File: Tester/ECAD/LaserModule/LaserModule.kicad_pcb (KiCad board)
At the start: 2 copper layers, 16 parts, among them J1 Conn_01x04_Male, Q1 ZXMP6A17G, U1 MCP4716, U2 AD8601

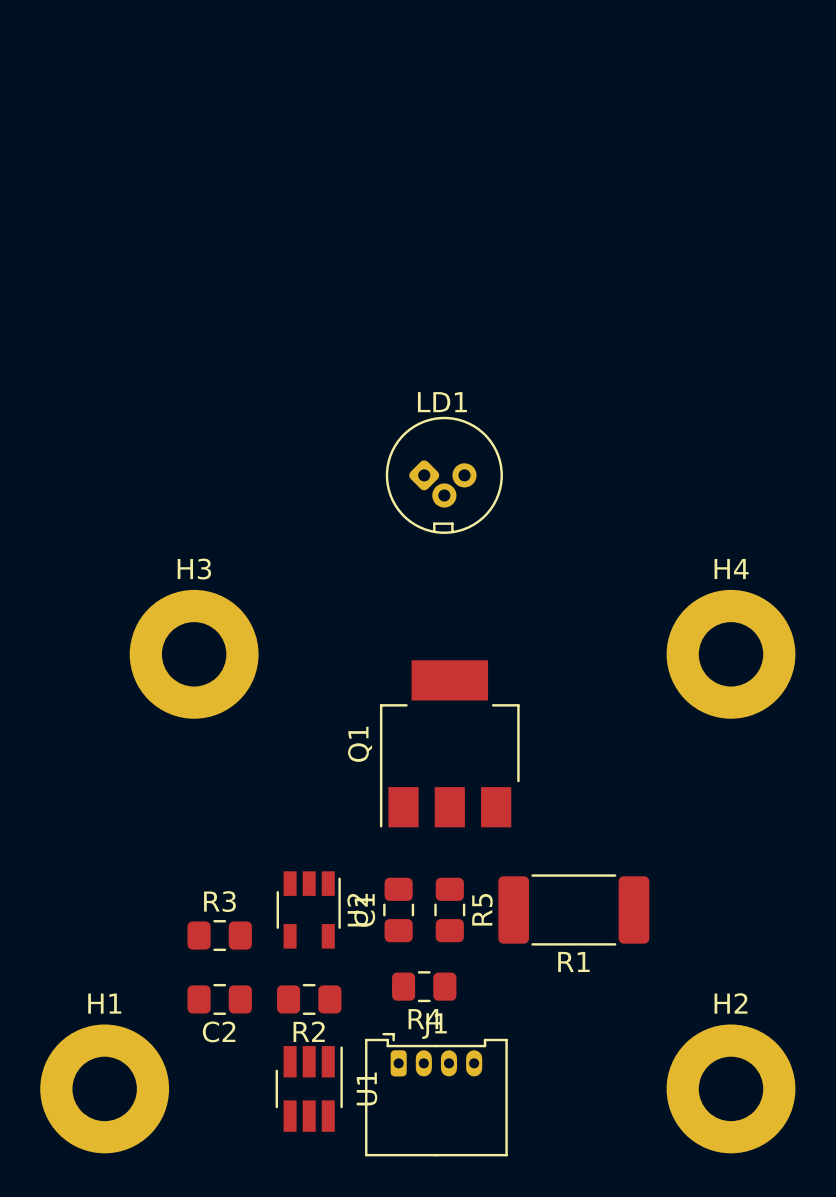
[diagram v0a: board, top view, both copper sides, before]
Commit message: Progressed laser module.
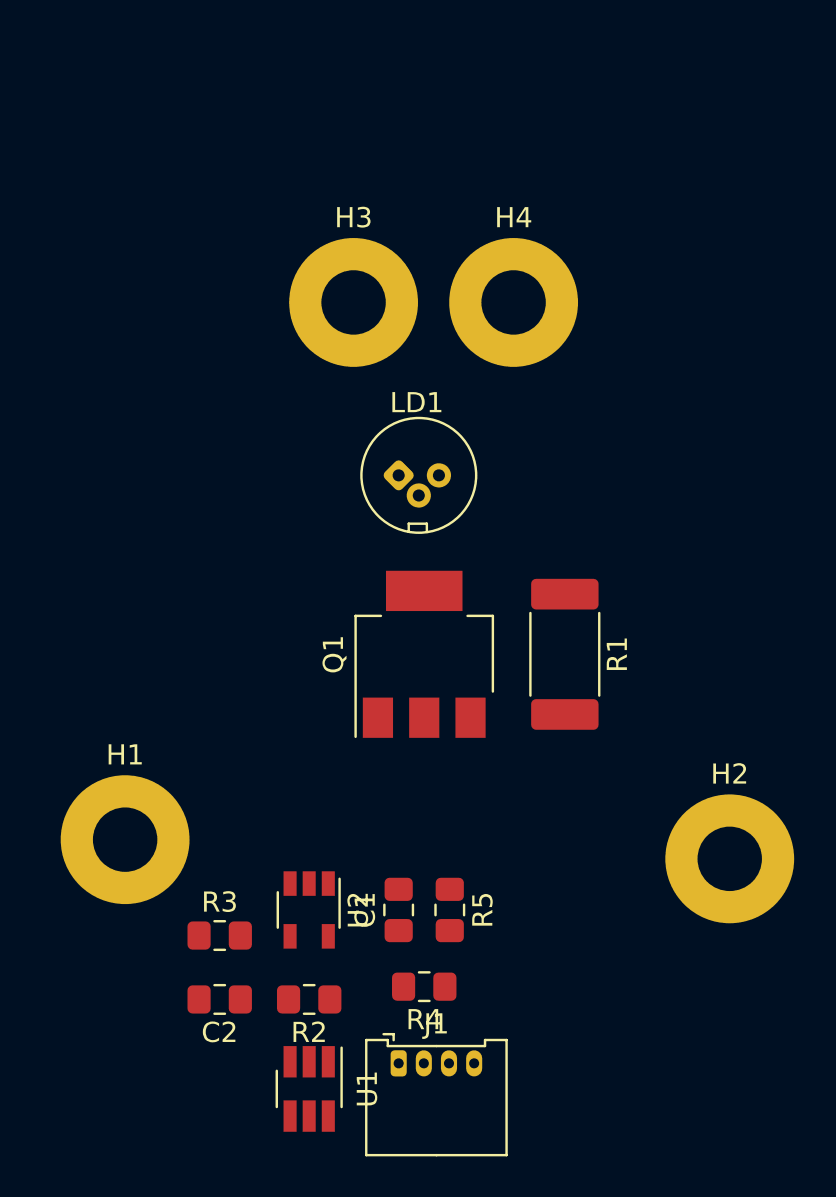
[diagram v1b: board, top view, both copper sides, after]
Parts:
- moved H4 20.5 mm to (147.3, 61.3)
- moved H3 19.2 mm to (139.4, 61.3)
- moved R1 12.7 mm to (149.9, 78.7), turned to 270 degrees
- moved H1 12.4 mm to (128.0, 87.9)
- moved H2 11.4 mm to (158.1, 88.9)
- moved Q1 4.62 mm to (142.9, 78.7)
- moved LD1 1.27 mm to (141.6, 69.8)
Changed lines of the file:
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@@
     (add_net "Net-(LD1-Pad1)")
+  )
+  (module MountingHole:MountingHole_3.2mm_M3_Pad (layer F.Cu)
+    (at 147.315001 61.260001)
+    (descr "Mounting Hole 3.2mm, M3")
+    (tags "mounting hole 3.2mm m3")
+    (attr virtual)
+    (fp_text reference H4 (at 0 -4.2) (layer F.SilkS)
+      (effects (font (size 1 1) (thickness 0.15)))
+    )
+    (fp_text value MountingHole (at 0 4.2) (layer F.Fab)
+      (effects (font (size 1 1) (thickness 0.15)))
+    )
+    (fp_circle (center 0 0) (end 3.45 0) (layer F.CrtYd) (width 0.05))
+    (fp_circle (center 0 0) (end 3.2 0) (layer Cmts.User) (width 0.15))
+    (fp_text user %R (at 0.3 0) (layer F.Fab)
+      (effects (font (size 1 1) (thickness 0.15)))
+    )
+    (pad 1 thru_hole circle (at 0 0) (size 6.4 6.4) (drill 3.2) (layers *.Cu *.Mask))
+  )
+  (module MountingHole:MountingHole_3.2mm_M3_Pad (layer F.Cu)
+    (at 139.365001 61.260001)
+    (descr "Mounting Hole 3.2mm, M3")
+    (tags "mounting hole 3.2mm m3")
+    (attr virtual)
+    (fp_text reference H3 (at 0 -4.2) (layer F.SilkS)
+      (effects (font (size 1 1) (thickness 0.15)))
+    )
+    (fp_text value MountingHole (at 0 4.2) (layer F.Fab)
+      (effects (font (size 1 1) (thickness 0.15)))
+    )
+    (fp_circle (center 0 0) (end 3.45 0) (layer F.CrtYd) (width 0.05))
+    (fp_circle (center 0 0) (end 3.2 0) (layer Cmts.User) (width 0.15))
+    (fp_text user %R (at 0.3 0) (layer F.Fab)
+      (effects (font (size 1 1) (thickness 0.15)))
+    )
+    (pad 1 thru_hole circle (at 0 0) (size 6.4 6.4) (drill 3.2) (layers *.Cu *.Mask))
   )
   (module Package_TO_SOT_SMD:SOT-23-6_Handsoldering (layer F.Cu)
@@
   )
   (module OptoDevice:LaserDiode_TO18-D5.6-3 (layer F.Cu)
-    (at 142.875 69.85)
+    (at 141.605 69.85)
     (descr "Laser Diode, TO18-like (D=5.6mm), 3pin")
     (tags "Laser Diode TO18-like")
@@
   )
   (module Resistor_SMD:R_2512_6332Metric_Pad1.52x3.35mm_HandSolder (layer F.Cu)
-    (at 150.3075 91.44 180)
+    (at 149.86 78.74 270)
     (descr "Resistor SMD 2512 (6332 Metric), square (rectangular) end terminal, IPC_7351 nominal with elongated pad for handsoldering. (Body size source: http://www.tortai-tech.com/upload/download/2011102023233369053.pdf), generated with kicad-footprint-generator")
     (tags "resistor handsolder")
     (attr smd)
-    (fp_text reference R1 (at 0 -2.62) (layer F.SilkS)
-      (effects (font (size 1 1) (thickness 0.15)))
-    )
-    (fp_text value 12R (at 0 2.62) (layer F.Fab)
-      (effects (font (size 1 1) (thickness 0.15)))
-    )
-    (fp_text user %R (at 0 0) (layer F.Fab)
+    (fp_text reference R1 (at 0 -2.62 90) (layer F.SilkS)
+      (effects (font (size 1 1) (thickness 0.15)))
+    )
+    (fp_text value 12R (at 0 2.62 90) (layer F.Fab)
+      (effects (font (size 1 1) (thickness 0.15)))
+    )
+    (fp_text user %R (at 0 0 90) (layer F.Fab)
       (effects (font (size 1 1) (thickness 0.15)))
     )
@@
     (fp_line (start -3.15 -1.6) (end 3.15 -1.6) (layer F.Fab) (width 0.1))
     (fp_line (start -3.15 1.6) (end -3.15 -1.6) (layer F.Fab) (width 0.1))
-    (pad 2 smd roundrect (at 2.9875 0 180) (size 1.525 3.35) (layers F.Cu F.Paste F.Mask) (roundrect_rratio 0.163934)
+    (pad 2 smd roundrect (at 2.9875 0 270) (size 1.525 3.35) (layers F.Cu F.Paste F.Mask) (roundrect_rratio 0.163934)
       (net 10 /S))
-    (pad 1 smd roundrect (at -2.9875 0 180) (size 1.525 3.35) (layers F.Cu F.Paste F.Mask) (roundrect_rratio 0.163934)
+    (pad 1 smd roundrect (at -2.9875 0 270) (size 1.525 3.35) (layers F.Cu F.Paste F.Mask) (roundrect_rratio 0.163934)
       (net 2 +5C))
     (model ${KISYS3DMOD}/Resistor_SMD.3dshapes/R_2512_6332Metric.wrl
@@
   )
   (module Package_TO_SOT_SMD:SOT-223-3_TabPin2 (layer F.Cu)
-    (at 144.145 83.185 90)
+    (at 142.875 78.74 90)
     (descr "module CMS SOT223 4 pins")
     (tags "CMS SOT")
@@
   )
   (module MountingHole:MountingHole_3.2mm_M3_Pad (layer F.Cu)
-    (at 158.115 78.74)
-    (descr "Mounting Hole 3.2mm, M3")
-    (tags "mounting hole 3.2mm m3")
-    (attr virtual)
-    (fp_text reference H4 (at 0 -4.2) (layer F.SilkS)
-      (effects (font (size 1 1) (thickness 0.15)))
-    )
-    (fp_text value MountingHole (at 0 4.2) (layer F.Fab)
-      (effects (font (size 1 1) (thickness 0.15)))
-    )
-    (fp_circle (center 0 0) (end 3.45 0) (layer F.CrtYd) (width 0.05))
-    (fp_circle (center 0 0) (end 3.2 0) (layer Cmts.User) (width 0.15))
-    (fp_text user %R (at 0.3 0) (layer F.Fab)
-      (effects (font (size 1 1) (thickness 0.15)))
-    )
-    (pad 1 thru_hole circle (at 0 0) (size 6.4 6.4) (drill 3.2) (layers *.Cu *.Mask))
-  )
-  (module MountingHole:MountingHole_3.2mm_M3_Pad (layer F.Cu)
-    (at 131.445 78.74)
-    (descr "Mounting Hole 3.2mm, M3")
-    (tags "mounting hole 3.2mm m3")
-    (attr virtual)
-    (fp_text reference H3 (at 0 -4.2) (layer F.SilkS)
-      (effects (font (size 1 1) (thickness 0.15)))
-    )
-    (fp_text value MountingHole (at 0 4.2) (layer F.Fab)
-      (effects (font (size 1 1) (thickness 0.15)))
-    )
-    (fp_circle (center 0 0) (end 3.45 0) (layer F.CrtYd) (width 0.05))
-    (fp_circle (center 0 0) (end 3.2 0) (layer Cmts.User) (width 0.15))
-    (fp_text user %R (at 0.3 0) (layer F.Fab)
-      (effects (font (size 1 1) (thickness 0.15)))
-    )
-    (pad 1 thru_hole circle (at 0 0) (size 6.4 6.4) (drill 3.2) (layers *.Cu *.Mask))
-  )
-  (module MountingHole:MountingHole_3.2mm_M3_Pad (layer F.Cu)
-    (at 158.115 100.33)
+    (at 158.0515 88.9)
     (descr "Mounting Hole 3.2mm, M3")
     (tags "mounting hole 3.2mm m3")
@@
   )
   (module MountingHole:MountingHole_3.2mm_M3_Pad (layer F.Cu)
-    (at 127 100.33)
+    (at 128.016 87.9475)
     (descr "Mounting Hole 3.2mm, M3")
     (tags "mounting hole 3.2mm m3")

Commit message: Minor updates.
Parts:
- removed H3, H4: MountingHole, MountingHole:MountingHole_3.2mm_M3_Pad
- LD1: moved to B.Cu
- moved U1 1.91 mm to (135.3, 100.3)
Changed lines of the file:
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@@
     (tracks 0)
     (zones 0)
-    (modules 16)
+    (modules 14)
     (nets 12)
   )
@@
     (add_net "Net-(LD1-Pad1)")
   )
-  (module MountingHole:MountingHole_3.2mm_M3_Pad (layer F.Cu)
-    (at 147.315001 61.260001)
-    (descr "Mounting Hole 3.2mm, M3")
-    (tags "mounting hole 3.2mm m3")
-    (attr virtual)
-    (fp_text reference H4 (at 0 -4.2) (layer F.SilkS)
-      (effects (font (size 1 1) (thickness 0.15)))
-    )
-    (fp_text value MountingHole (at 0 4.2) (layer F.Fab)
-      (effects (font (size 1 1) (thickness 0.15)))
-    )
-    (fp_circle (center 0 0) (end 3.45 0) (layer F.CrtYd) (width 0.05))
-    (fp_circle (center 0 0) (end 3.2 0) (layer Cmts.User) (width 0.15))
-    (fp_text user %R (at 0.3 0) (layer F.Fab)
-      (effects (font (size 1 1) (thickness 0.15)))
-    )
-    (pad 1 thru_hole circle (at 0 0) (size 6.4 6.4) (drill 3.2) (layers *.Cu *.Mask))
-  )
-  (module MountingHole:MountingHole_3.2mm_M3_Pad (layer F.Cu)
-    (at 139.365001 61.260001)
-    (descr "Mounting Hole 3.2mm, M3")
-    (tags "mounting hole 3.2mm m3")
-    (attr virtual)
-    (fp_text reference H3 (at 0 -4.2) (layer F.SilkS)
-      (effects (font (size 1 1) (thickness 0.15)))
-    )
-    (fp_text value MountingHole (at 0 4.2) (layer F.Fab)
-      (effects (font (size 1 1) (thickness 0.15)))
-    )
-    (fp_circle (center 0 0) (end 3.45 0) (layer F.CrtYd) (width 0.05))
-    (fp_circle (center 0 0) (end 3.2 0) (layer Cmts.User) (width 0.15))
-    (fp_text user %R (at 0.3 0) (layer F.Fab)
-      (effects (font (size 1 1) (thickness 0.15)))
-    )
-    (pad 1 thru_hole circle (at 0 0) (size 6.4 6.4) (drill 3.2) (layers *.Cu *.Mask))
-  )
   (module Package_TO_SOT_SMD:SOT-23-6_Handsoldering (layer F.Cu)
-    (at 137.16 100.33 270)
+    (at 135.255 100.33 270)
     (descr "6-pin SOT-23 package, Handsoldering")
     (tags "SOT-23-6 Handsoldering")
@@
     )
   )
-  (module OptoDevice:LaserDiode_TO18-D5.6-3 (layer F.Cu)
+  (module OptoDevice:LaserDiode_TO18-D5.6-3 (layer B.Cu)
     (at 141.605 69.85)
     (descr "Laser Diode, TO18-like (D=5.6mm), 3pin")
     (tags "Laser Diode TO18-like")
-    (fp_text reference LD1 (at 0.9 -3.6) (layer F.SilkS)
-      (effects (font (size 1 1) (thickness 0.15)))
+    (fp_text reference LD1 (at 0.9 3.6) (layer B.SilkS)
+      (effects (font (size 1 1) (thickness 0.15)) (justify mirror))
     )
-    (fp_text value SLD3134VL (at 1 3.8) (layer F.Fab)
-      (effects (font (size 1 1) (thickness 0.15)))
+    (fp_text value SLD3134VL (at 1 -3.8) (layer B.Fab)
+      (effects (font (size 1 1) (thickness 0.15)) (justify mirror))
     )
-    (fp_circle (center 1 0) (end -1.85 0) (layer F.SilkS) (width 0.12))
-    (fp_circle (center 1 0) (end 3.2 0) (layer F.Fab) (width 0.1))
-    (fp_circle (center 1 0) (end 2.8 0) (layer F.Fab) (width 0.1))
-    (fp_circle (center 1.02 0.01) (end 3.85 1.49) (layer F.CrtYd) (width 0.05))
-    (fp_circle (center 1 0) (end -1.8 0) (layer F.Fab) (width 0.1))
-    (fp_line (start 1.4 2.4) (end 1.4 2.7) (layer F.Fab) (width 0.1))
-    (fp_line (start 0.5 2.4) (end 1.4 2.4) (layer F.Fab) (width 0.1))
-    (fp_line (start 0.5 2.7) (end 0.5 2.4) (layer F.Fab) (width 0.1))
-    (fp_line (start 3.4 0) (end 3.7 0.4) (layer F.Fab) (width 0.1))
-    (fp_line (start 3.7 -0.4) (end 3.4 0) (layer F.Fab) (width 0.1))
-    (fp_line (start -1.4 0) (end -1.7 -0.4) (layer F.Fab) (width 0.1))
-    (fp_line (start -1.4 0) (end -1.7 0.4) (layer F.Fab) (width 0.1))
-    (fp_line (start 1.4 2.4) (end 1.4 2.8) (layer F.SilkS) (width 0.12))
-    (fp_line (start 0.5 2.4) (end 1.4 2.4) (layer F.SilkS) (width 0.12))
-    (fp_line (start 0.5 2.8) (end 0.5 2.4) (layer F.SilkS) (width 0.12))
-    (fp_text user %R (at 0.9 -3.6) (layer F.Fab)
-      (effects (font (size 1 1) (thickness 0.15)))
+    (fp_circle (center 1 0) (end -1.85 0) (layer B.SilkS) (width 0.12))
+    (fp_circle (center 1 0) (end 3.2 0) (layer B.Fab) (width 0.1))
+    (fp_circle (center 1 0) (end 2.8 0) (layer B.Fab) (width 0.1))
+    (fp_circle (center 1.02 -0.01) (end 3.85 -1.49) (layer B.CrtYd) (width 0.05))
+    (fp_circle (center 1 0) (end -1.8 0) (layer B.Fab) (width 0.1))
+    (fp_line (start 1.4 -2.4) (end 1.4 -2.7) (layer B.Fab) (width 0.1))
+    (fp_line (start 0.5 -2.4) (end 1.4 -2.4) (layer B.Fab) (width 0.1))
+    (fp_line (start 0.5 -2.7) (end 0.5 -2.4) (layer B.Fab) (width 0.1))
+    (fp_line (start 3.4 0) (end 3.7 -0.4) (layer B.Fab) (width 0.1))
+    (fp_line (start 3.7 0.4) (end 3.4 0) (layer B.Fab) (width 0.1))
+    (fp_line (start -1.4 0) (end -1.7 0.4) (layer B.Fab) (width 0.1))
+    (fp_line (start -1.4 0) (end -1.7 -0.4) (layer B.Fab) (width 0.1))
+    (fp_line (start 1.4 -2.4) (end 1.4 -2.8) (layer B.SilkS) (width 0.12))
+    (fp_line (start 0.5 -2.4) (end 1.4 -2.4) (layer B.SilkS) (width 0.12))
+    (fp_line (start 0.5 -2.8) (end 0.5 -2.4) (layer B.SilkS) (width 0.12))
+    (fp_text user %R (at 0.9 3.6) (layer B.Fab)
+      (effects (font (size 1 1) (thickness 0.15)) (justify mirror))
     )
     (pad 3 thru_hole circle (at 2 0) (size 1.2 1.2) (drill 0.6) (layers *.Cu *.Mask)
       (net 9 /D))
-    (pad 2 thru_hole circle (at 1 1) (size 1.2 1.2) (drill 0.6) (layers *.Cu *.Mask)
+    (pad 2 thru_hole circle (at 1 -1) (size 1.2 1.2) (drill 0.6) (layers *.Cu *.Mask)
       (net 1 GND))
-    (pad 1 thru_hole roundrect (at 0 0 45) (size 1.2 1.2) (drill 0.6) (layers *.Cu *.Mask) (roundrect_rratio 0.208)
+    (pad 1 thru_hole roundrect (at 0 0 315) (size 1.2 1.2) (drill 0.6) (layers *.Cu *.Mask) (roundrect_rratio 0.208)
       (net 5 "Net-(LD1-Pad1)"))
     (model ${KISYS3DMOD}/OptoDevice.3dshapes/LaserDiode_TO18-D5.6-3.wrl

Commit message: Updated DRC.
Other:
- net class Default: clearance 0.2 -> 0.21; via_dia 0.8 -> 0.6; via_drill 0.4 -> 0.3
- net class Power added: clearance 0.21, trace_width 0.5, via_dia 0.8, via_drill 0.4
- rule pad_to_mask_clearance: 0.051 -> 0.0508
- rule trace_clearance: 0.2 -> 0.21
- rule trace_min: 0.2 -> 0.1524
- rule via_min_drill: 0.3 -> 0.254
- rule via_min_size: 0.4 -> 0.508
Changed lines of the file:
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@@
   (setup
     (last_trace_width 0.25)
-    (trace_clearance 0.2)
+    (trace_clearance 0.21)
     (zone_clearance 0.508)
     (zone_45_only no)
-    (trace_min 0.2)
-    (via_size 0.8)
-    (via_drill 0.4)
-    (via_min_size 0.4)
-    (via_min_drill 0.3)
-    (uvia_size 0.3)
-    (uvia_drill 0.1)
+    (trace_min 0.1524)
+    (via_size 0.6)
+    (via_drill 0.3)
+    (via_min_size 0.508)
+    (via_min_drill 0.254)
+    (uvia_size 0.8)
+    (uvia_drill 0.4)
     (uvias_allowed no)
-    (uvia_min_size 0.2)
-    (uvia_min_drill 0.1)
+    (uvia_min_size 0.508)
+    (uvia_min_drill 0.254)
     (edge_width 0.05)
     (segment_width 0.2)
@@
     (pad_size 1.524 1.524)
     (pad_drill 0.762)
-    (pad_to_mask_clearance 0.051)
-    (solder_mask_min_width 0.25)
+    (pad_to_mask_clearance 0.0508)
     (aux_axis_origin 0 0)
     (visible_elements 7FFFFFFF)
@@
   (net 11 /VOUT)
   (net_class Default "This is the default net class."
-    (clearance 0.2)
+    (clearance 0.21)
     (trace_width 0.25)
+    (via_dia 0.6)
+    (via_drill 0.3)
+    (uvia_dia 0.8)
+    (uvia_drill 0.4)
+    (add_net /G)
+    (add_net /SCL)
+    (add_net /SDA)
+    (add_net "Net-(LD1-Pad1)")
+  )
+  (net_class Power ""
+    (clearance 0.21)
+    (trace_width 0.5)
     (via_dia 0.8)
     (via_drill 0.4)
-    (uvia_dia 0.3)
-    (uvia_drill 0.1)
+    (uvia_dia 0.8)
+    (uvia_drill 0.4)
     (add_net +5C)
     (add_net /D)
-    (add_net /G)
     (add_net /S)
-    (add_net /SCL)
-    (add_net /SDA)
     (add_net /V+)
     (add_net /V-)
     (add_net /VOUT)
     (add_net GND)
-    (add_net "Net-(LD1-Pad1)")
   )
   (module Package_TO_SOT_SMD:SOT-23-6_Handsoldering (layer F.Cu)

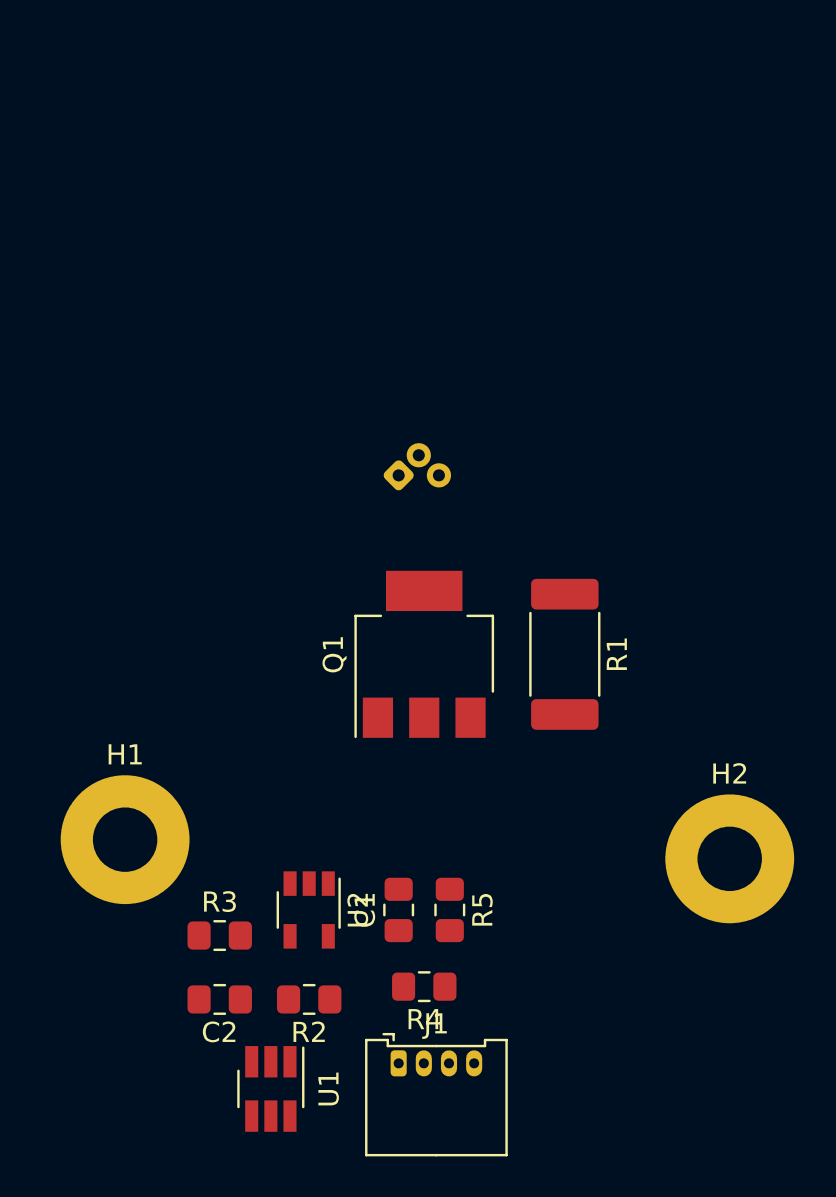
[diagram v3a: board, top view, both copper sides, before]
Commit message: Progressed laser module layout.
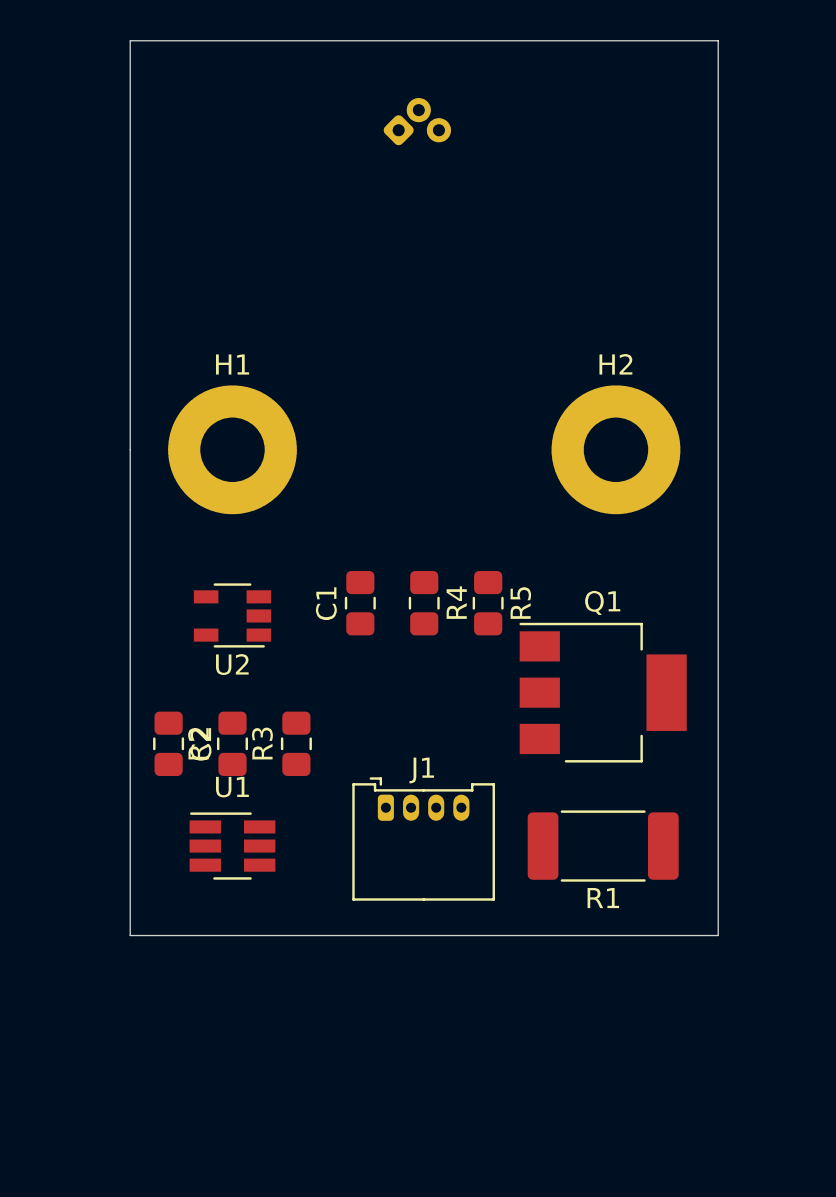
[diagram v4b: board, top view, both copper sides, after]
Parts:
- moved H2 21.1 mm to (152.4, 68.6)
- moved H1 20.1 mm to (133.3, 68.6)
- moved R4 19.0 mm to (142.9, 76.2), turned to 270 degrees
- moved LD1 17.1 mm to (141.6, 52.7)
- moved C1 15.4 mm to (139.7, 76.2)
- moved R5 15.4 mm to (146.1, 76.2)
- moved U2 15.1 mm to (133.3, 76.8), turned to 180 degrees
- moved R2 13.3 mm to (133.3, 83.2), turned to 90 degrees
- moved C2 13.0 mm to (130.2, 83.2), turned to 270 degrees
- moved J1 12.7 mm to (141.0, 86.4)
- moved U1 12.2 mm to (133.3, 88.3), turned to 0 degrees
- moved R3 10.3 mm to (136.5, 83.2), turned to 90 degrees
- moved R1 9.71 mm to (151.8, 88.3), turned to 180 degrees
- moved Q1 9.09 mm to (151.8, 80.6), turned to 0 degrees
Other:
- board outline added: 29.2 x 44.4 mm
- net class Power: trace_width 0.5 -> 0.7
